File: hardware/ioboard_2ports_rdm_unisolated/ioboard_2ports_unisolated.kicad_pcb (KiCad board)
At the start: 2 copper layers, 106 x 55 mm, 32 parts, among them J1 Conn_02x06_Odd_Even, J12 Conn_01x03, J2 XLR3, J3 XLR3, J4 8P8C, J5 8P8C, J6 Conn_01x03, J8 XLR3, J9 XLR3, U1 M24C64-RMN6TP, U2 SP3485EN, U3 AMS1117-3.3, U4 SP3485EN

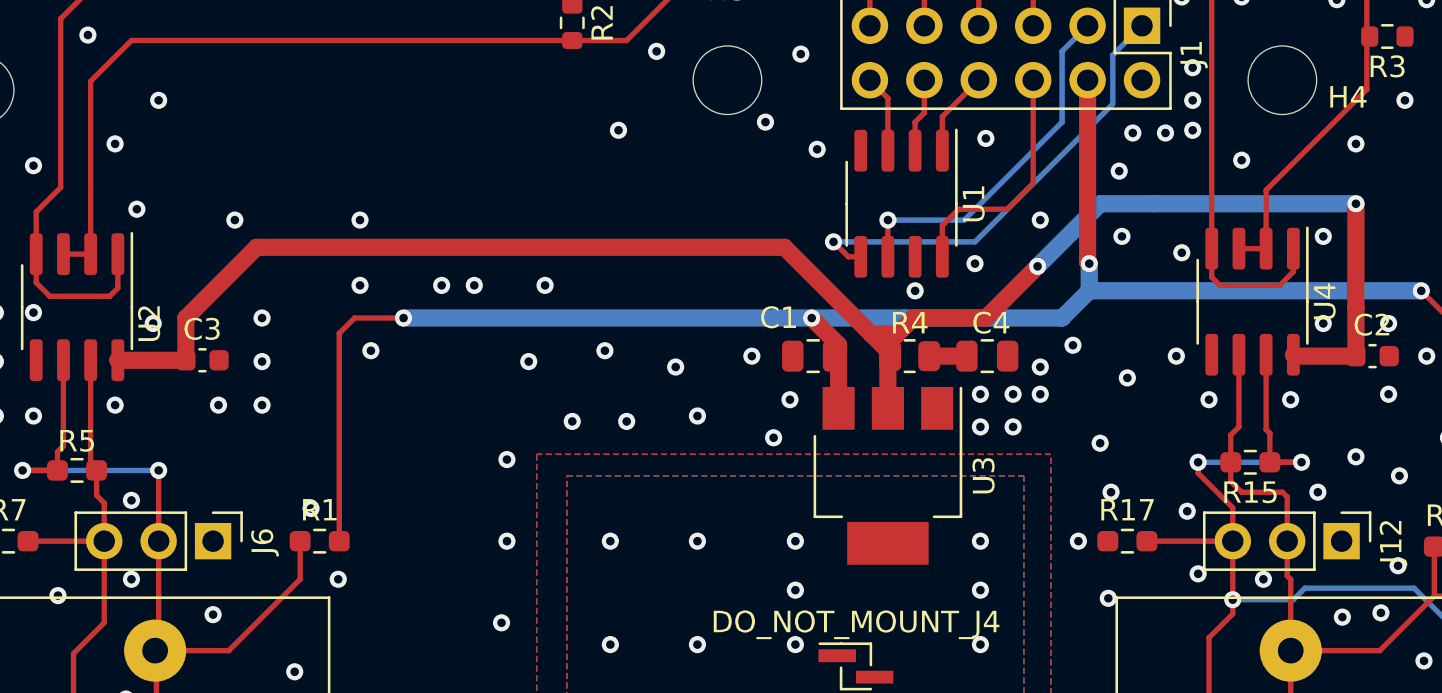
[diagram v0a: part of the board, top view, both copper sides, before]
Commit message: Update all footprints and ignore all other DRC warning on ioboards
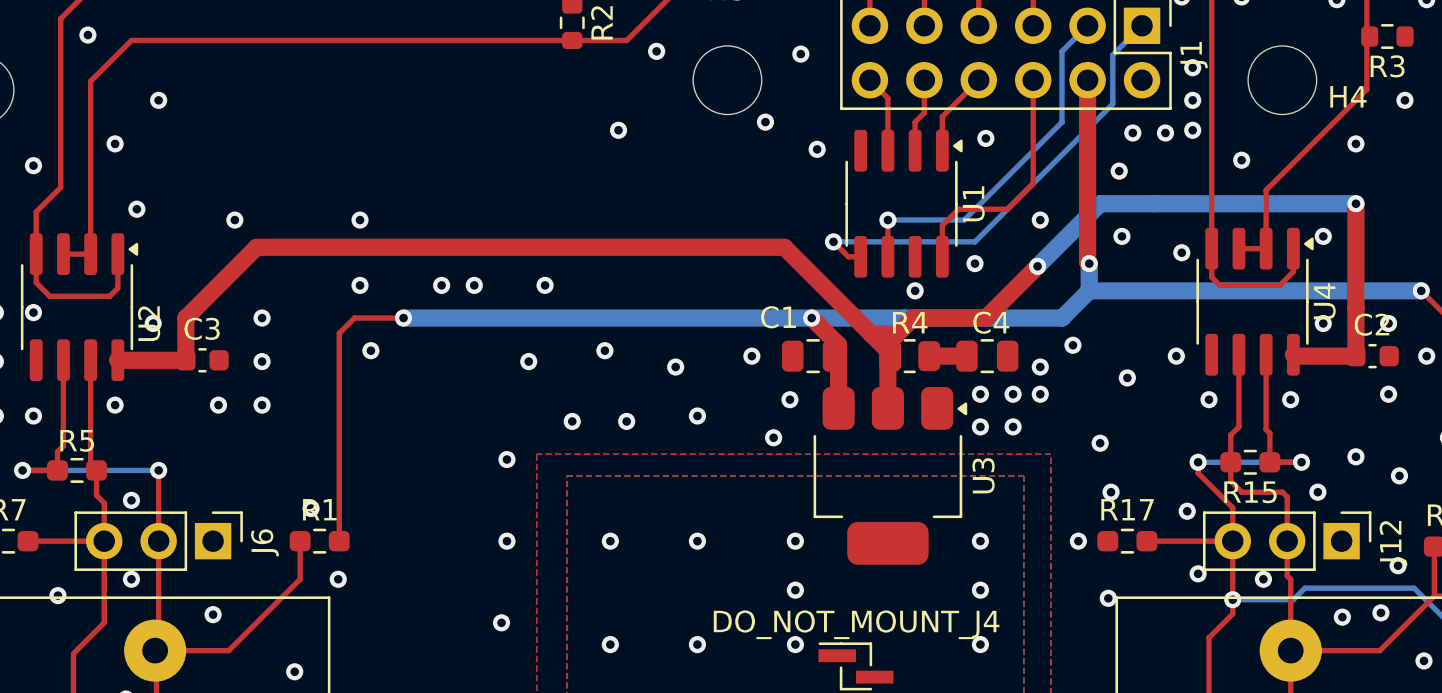
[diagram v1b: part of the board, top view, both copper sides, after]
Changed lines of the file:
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@@
 			(pintype "passive")
 		)
-		(model "${KISYS3DMOD}/Connector_PinHeader_2.54mm.3dshapes/PinHeader_2x06_P2.54mm_Vertical.wrl"
+		(model "${KICAD8_3DMODEL_DIR}/Connector_PinHeader_2.54mm.3dshapes/PinHeader_2x06_P2.54mm_Vertical.wrl"
 			(offset
 				(xyz 0 0 0)
@@
 			(pintype "passive")
 		)
-		(model "${KISYS3DMOD}/Resistor_SMD.3dshapes/R_0603_1608Metric.wrl"
+		(model "${KICAD8_3DMODEL_DIR}/Resistor_SMD.3dshapes/R_0603_1608Metric.wrl"
 			(offset
 				(xyz 0 0 0)
@@
 		(fp_line
 			(start 0 -2.56)
-			(end -3.45 -2.56)
+			(end -1.95 -2.56)
 			(stroke
 				(width 0.12)
@@
 			(layer "F.SilkS")
 		)
+		(fp_poly
+			(pts
+				(xy -2.7 -2.465) (xy -2.94 -2.795) (xy -2.46 -2.795) (xy -2.7 -2.465)
+			)
+			(stroke
+				(width 0.12)
+				(type solid)
+			)
+			(fill solid)
+			(layer "F.SilkS")
+		)
 		(fp_line
 			(start -3.7 2.7)
@@
 			(pintype "power_in")
 		)
-		(model "${KISYS3DMOD}/Package_SO.3dshapes/SOIC-8_3.9x4.9mm_P1.27mm.wrl"
+		(model "${KICAD8_3DMODEL_DIR}/Package_SO.3dshapes/SOIC-8_3.9x4.9mm_P1.27mm.wrl"
 			(offset
 				(xyz 0 0 0)
@@
 			(pintype "passive")
 		)
-		(model "${KISYS3DMOD}/Resistor_SMD.3dshapes/R_0603_1608Metric.wrl"
+		(model "${KICAD8_3DMODEL_DIR}/Resistor_SMD.3dshapes/R_0603_1608Metric.wrl"
 			(offset
 				(xyz 0 0 0)
@@
 			(pintype "passive")
 		)
-		(model "${KISYS3DMOD}/Resistor_SMD.3dshapes/R_0603_1608Metric.wrl"
+		(model "${KICAD8_3DMODEL_DIR}/Resistor_SMD.3dshapes/R_0603_1608Metric.wrl"
 			(offset
 				(xyz 0 0 0)
@@
 			(pintype "passive")
 		)
-		(model "${KISYS3DMOD}/Capacitor_SMD.3dshapes/C_0603_1608Metric.wrl"
+		(model "${KICAD8_3DMODEL_DIR}/Capacitor_SMD.3dshapes/C_0603_1608Metric.wrl"
 			(offset
 				(xyz 0 0 0)
@@
 		(fp_line
 			(start 0 -2.56)
-			(end -3.45 -2.56)
+			(end -1.95 -2.56)
 			(stroke
 				(width 0.12)
@@
 			(layer "F.SilkS")
 		)
+		(fp_poly
+			(pts
+				(xy -2.7 -2.465) (xy -2.94 -2.795) (xy -2.46 -2.795) (xy -2.7 -2.465)
+			)
+			(stroke
+				(width 0.12)
+				(type solid)
+			)
+			(fill solid)
+			(layer "F.SilkS")
+		)
 		(fp_line
 			(start -3.7 2.7)
@@
 			(pintype "power_in")
 		)
-		(model "${KISYS3DMOD}/Package_SO.3dshapes/SOIC-8_3.9x4.9mm_P1.27mm.wrl"
+		(model "${KICAD8_3DMODEL_DIR}/Package_SO.3dshapes/SOIC-8_3.9x4.9mm_P1.27mm.wrl"
 			(offset
 				(xyz 0 0 0)
@@
 			(pintype "passive")
 		)
-		(model "${KISYS3DMOD}/Connector_PinHeader_2.54mm.3dshapes/PinHeader_1x03_P2.54mm_Vertical.wrl"
+		(model "${KICAD8_3DMODEL_DIR}/Connector_PinHeader_2.54mm.3dshapes/PinHeader_1x03_P2.54mm_Vertical.wrl"
 			(offset
 				(xyz 0 0 0)
@@
 			(pintype "passive")
 		)
-		(model "${KICAD6_3DMODEL_DIR}/Connector_Audio.3dshapes/Jack_XLR_Neutrik_NC3FAAH_Horizontal.wrl"
+		(model "${KICAD8_3DMODEL_DIR}/Connector_Audio.3dshapes/Jack_XLR_Neutrik_NC3FAAH_Horizontal.wrl"
 			(offset
 				(xyz 0 0 0)
@@
 			(pintype "passive")
 		)
-		(model "${KICAD6_3DMODEL_DIR}/Connector_Audio.3dshapes/Jack_XLR_Neutrik_NC3FAAH_Horizontal.wrl"
+		(model "${KICAD8_3DMODEL_DIR}/Connector_Audio.3dshapes/Jack_XLR_Neutrik_NC3FAAH_Horizontal.wrl"
 			(offset
 				(xyz 0 0 0)
@@
 			(pintype "passive")
 		)
-		(model "${KISYS3DMOD}/Connector_PinHeader_2.54mm.3dshapes/PinHeader_1x03_P2.54mm_Vertical.wrl"
+		(model "${KICAD8_3DMODEL_DIR}/Connector_PinHeader_2.54mm.3dshapes/PinHeader_1x03_P2.54mm_Vertical.wrl"
 			(offset
 				(xyz 0 0 0)
@@
 			(pintype "passive")
 		)
-		(model "${KISYS3DMOD}/Resistor_SMD.3dshapes/R_0603_1608Metric.wrl"
+		(model "${KICAD8_3DMODEL_DIR}/Resistor_SMD.3dshapes/R_0603_1608Metric.wrl"
 			(offset
 				(xyz 0 0 0)
@@
 			(pintype "passive")
 		)
-		(model "${KISYS3DMOD}/Resistor_SMD.3dshapes/R_0603_1608Metric.wrl"
+		(model "${KICAD8_3DMODEL_DIR}/Resistor_SMD.3dshapes/R_0603_1608Metric.wrl"
 			(offset
 				(xyz 0 0 0)
@@
 			(pintype "passive")
 		)
-		(model "${KISYS3DMOD}/Resistor_SMD.3dshapes/R_0603_1608Metric.wrl"
+		(model "${KICAD8_3DMODEL_DIR}/Resistor_SMD.3dshapes/R_0603_1608Metric.wrl"
 			(offset
 				(xyz 0 0 0)
@@
 			(pintype "passive")
 		)
-		(model "${KISYS3DMOD}/Capacitor_SMD.3dshapes/C_0603_1608Metric.wrl"
+		(model "${KICAD8_3DMODEL_DIR}/Capacitor_SMD.3dshapes/C_0603_1608Metric.wrl"
 			(offset
 				(xyz 0 0 0)
@@
 		(fp_line
 			(start 0 -2.56)
-			(end -3.45 -2.56)
+			(end -1.95 -2.56)
 			(stroke
 				(width 0.12)
@@
 			(layer "F.SilkS")
 		)
+		(fp_poly
+			(pts
+				(xy -2.7 -2.465) (xy -2.94 -2.795) (xy -2.46 -2.795) (xy -2.7 -2.465)
+			)
+			(stroke
+				(width 0.12)
+				(type solid)
+			)
+			(fill solid)
+			(layer "F.SilkS")
+		)
 		(fp_line
 			(start -3.7 2.7)
@@
 			(pintype "power_in")
 		)
-		(model "${KISYS3DMOD}/Package_SO.3dshapes/SOIC-8_3.9x4.9mm_P1.27mm.wrl"
+		(model "${KICAD8_3DMODEL_DIR}/Package_SO.3dshapes/SOIC-8_3.9x4.9mm_P1.27mm.wrl"
 			(offset
 				(xyz 0 0 0)
@@
 			(pintype "passive")
 		)
-		(model "${KISYS3DMOD}/Resistor_SMD.3dshapes/R_0603_1608Metric.wrl"
+		(model "${KICAD8_3DMODEL_DIR}/Resistor_SMD.3dshapes/R_0603_1608Metric.wrl"
 			(offset
 				(xyz 0 0 0)
@@
 			(pintype "passive")
 		)
-		(model "${KISYS3DMOD}/Resistor_SMD.3dshapes/R_0603_1608Metric.wrl"
+		(model "${KICAD8_3DMODEL_DIR}/Resistor_SMD.3dshapes/R_0603_1608Metric.wrl"
 			(offset
 				(xyz 0 0 0)
@@
 			(pintype "passive")
 		)
-		(model "${KISYS3DMOD}/Resistor_SMD.3dshapes/R_0805_2012Metric.wrl"
+		(model "${KICAD8_3DMODEL_DIR}/Resistor_SMD.3dshapes/R_0805_2012Metric.wrl"
 			(offset
 				(xyz 0 0 0)
@@
 		)
 		(fp_line
-			(start -4.1 -3.41)
+			(start -1.85 -3.41)
 			(end 1.91 -3.41)
 			(stroke
@@
 			(layer "F.SilkS")
 		)
+		(fp_poly
+			(pts
+				(xy -3.13 -3.31) (xy -3.37 -3.64) (xy -2.89 -3.64) (xy -3.13 -3.31)
+			)
+			(stroke
+				(width 0.12)
+				(type solid)
+			)
+			(fill solid)
+			(layer "F.SilkS")
+		)
 		(fp_line
 			(start -4.4 3.6)
@@
 			)
 		)
-		(pad "1" smd rect
+		(pad "1" smd roundrect
 			(at -3.15 -2.3 270)
 			(size 2 1.5)
 			(layers "F.Cu" "F.Paste" "F.Mask")
+			(roundrect_rratio 0.25)
 			(net 9 "GND")
 			(pinfunction "GND")
 			(pintype "power_in")
 		)
-		(pad "2" smd rect
+		(pad "2" smd roundrect
 			(at -3.15 0 270)
 			(size 2 1.5)
 			(layers "F.Cu" "F.Paste" "F.Mask")
+			(roundrect_rratio 0.25)
 			(net 17 "/+3V3_INT")
 			(pinfunction "VO")
 			(pintype "power_out")
 		)
-		(pad "3" smd rect
+		(pad "3" smd roundrect
 			(at -3.15 2.3 270)
 			(size 2 1.5)
 			(layers "F.Cu" "F.Paste" "F.Mask")
+			(roundrect_rratio 0.25)
 			(net 7 "+5V")
 			(pinfunction "VI")
 			(pintype "power_in")
 		)
-		(pad "4" smd rect
+		(pad "4" smd roundrect
 			(at 3.15 0 270)
 			(size 2 3.8)
 			(layers "F.Cu" "F.Paste" "F.Mask")
+			(roundrect_rratio 0.25)
 		)
-		(model "${KISYS3DMOD}/Package_TO_SOT_SMD.3dshapes/SOT-223.wrl"
+		(model "${KICAD8_3DMODEL_DIR}/Package_TO_SOT_SMD.3dshapes/SOT-223.wrl"
 			(offset
 				(xyz 0 0 0)
@@
 			(pintype "passive")
 		)
-		(model "${KISYS3DMOD}/Capacitor_SMD.3dshapes/C_0805_2012Metric.wrl"
+		(model "${KICAD8_3DMODEL_DIR}/Capacitor_SMD.3dshapes/C_0805_2012Metric.wrl"
 			(offset
 				(xyz 0 0 0)
@@
 			(pintype "passive")
 		)
-		(model "${KISYS3DMOD}/Capacitor_SMD.3dshapes/C_0805_2012Metric.wrl"
+		(model "${KICAD8_3DMODEL_DIR}/Capacitor_SMD.3dshapes/C_0805_2012Metric.wrl"
 			(offset
 				(xyz 0 0 0)
@@
 			(layers "F.Cu" "F.Paste" "F.Mask")
 		)
-		(model "${KICAD6_3DMODEL_DIR}/Connector_PinHeader_1.00mm.3dshapes/PinHeader_1x02_P1.00mm_Vertical_SMD_Pin1Left.wrl"
+		(model "${KICAD8_3DMODEL_DIR}/Connector_PinHeader_1.00mm.3dshapes/PinHeader_1x02_P1.00mm_Vertical_SMD_Pin1Left.wrl"
 			(offset
 				(xyz 0 0 0)
